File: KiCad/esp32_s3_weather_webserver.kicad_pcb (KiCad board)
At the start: 4 copper layers, 85 x 75 mm, 129 parts, among them IC301 CP2102N-A02-GQFN28R, IC401 ESP32-S3-WROOM-1-N16R8, IC501 VEML7700-TT, IC502 DS3231MZ+TRL, J201 Barrel_Jack_Switch_Pin3Ring, J301 USB_C_Receptacle_USB2.0, J302 USB_C_Receptacle_USB2.0, J401 Conn_01x04_Pin, J402 Conn_01x04_Pin, J403 Conn_01x04_Pin, J404 TF-01A, J405 Conn_01x06_Pin, Q401 SS8050, Q402 SS8050, U201 AMS1117-3.3, U202 TLV62569DBV, U301 USBLC6-2SC6, U302 USBLC6-2SC6, U502 DS18B20, U503 LM35-LP, U504 DHT11

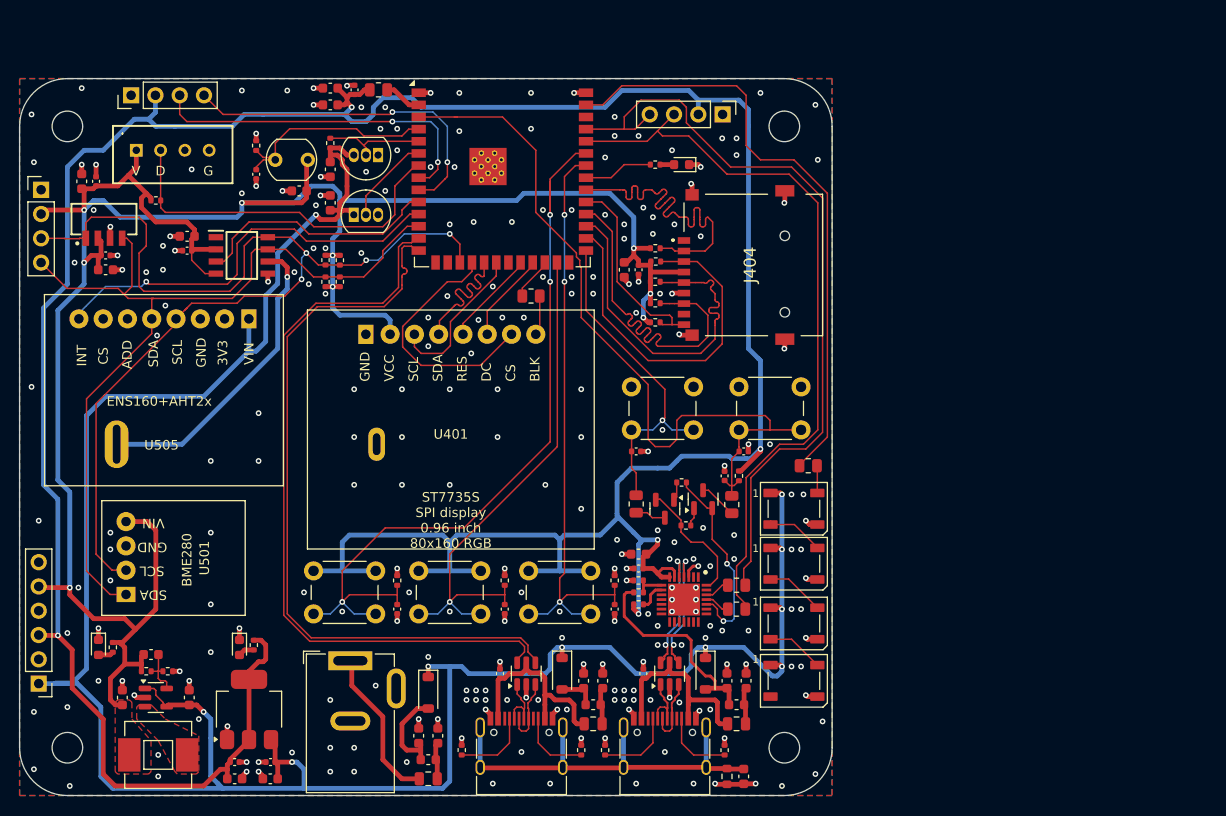
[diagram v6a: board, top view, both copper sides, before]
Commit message: Temperature sensor placement update
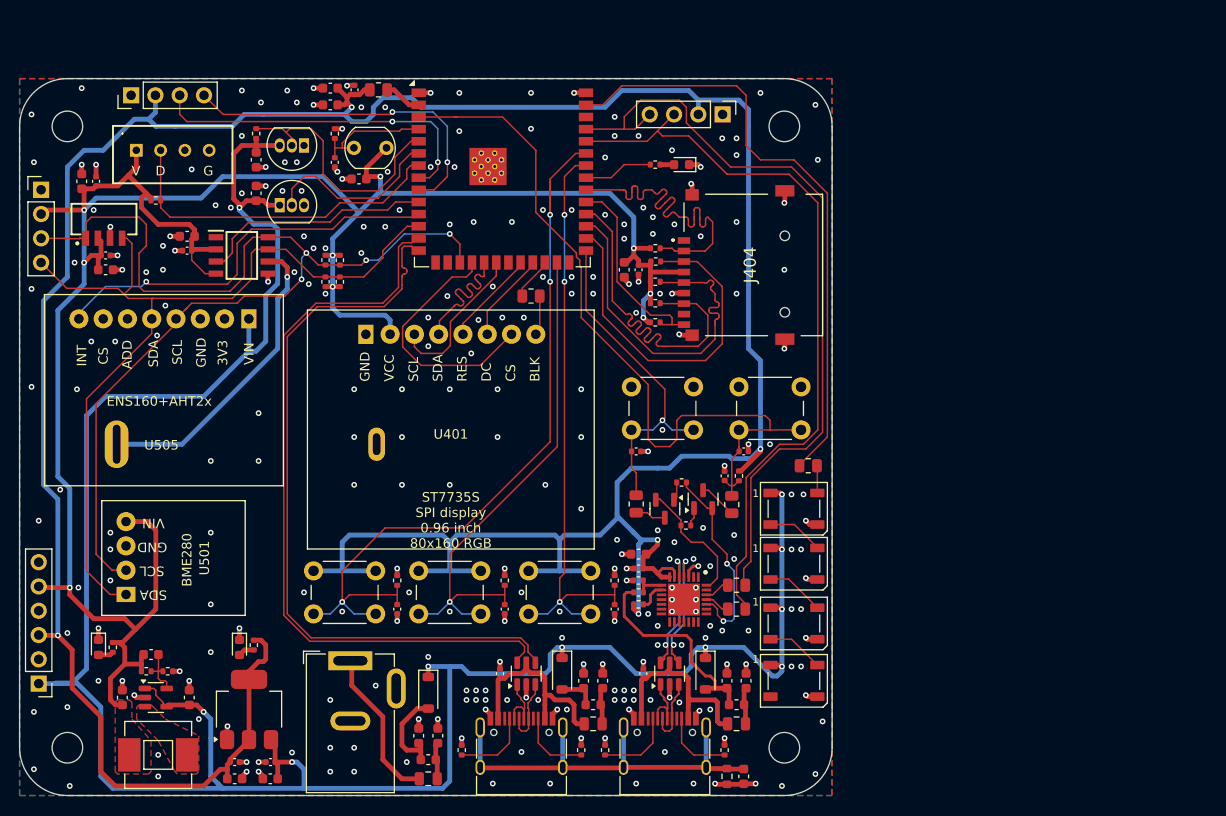
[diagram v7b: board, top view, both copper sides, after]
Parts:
- moved C502 8.32 mm to (58.0, 33.8)
- moved R501 8.32 mm to (58.0, 30.8)
- moved RLO501 8.32 mm to (60.0, 32.2)
- moved C505 7.81 mm to (49.8, 33.5)
- moved C506 7.81 mm to (49.8, 37.0)
- moved R504 7.81 mm to (49.8, 30.8)
- moved U502 7.81 mm to (54.8, 32.0)
- moved U503 7.81 mm to (52.2, 38.2)
- moved C501 6.37 mm to (60.5, 35.5)
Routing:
- net DS18B20: track 11.3 -> 26.9 mm
- net LM35: track 9.34 -> 19.1 mm
- net LDR: track 23.0 -> 13.5 mm
- net +3V3_PER: track 242.9 -> 238.3 mm
- net DHT11: track 38.2 -> 36.2 mm
- net +5V: track 249.9 -> 251.5 mm
- net DS3231_INT: track 26.0 -> 24.7 mm
- net ENS160_INT: track 43.6 -> 42.5 mm
- net GND: track 76.1 -> 76.0 mm, vias 258 -> 274

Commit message: Silk Screen updates
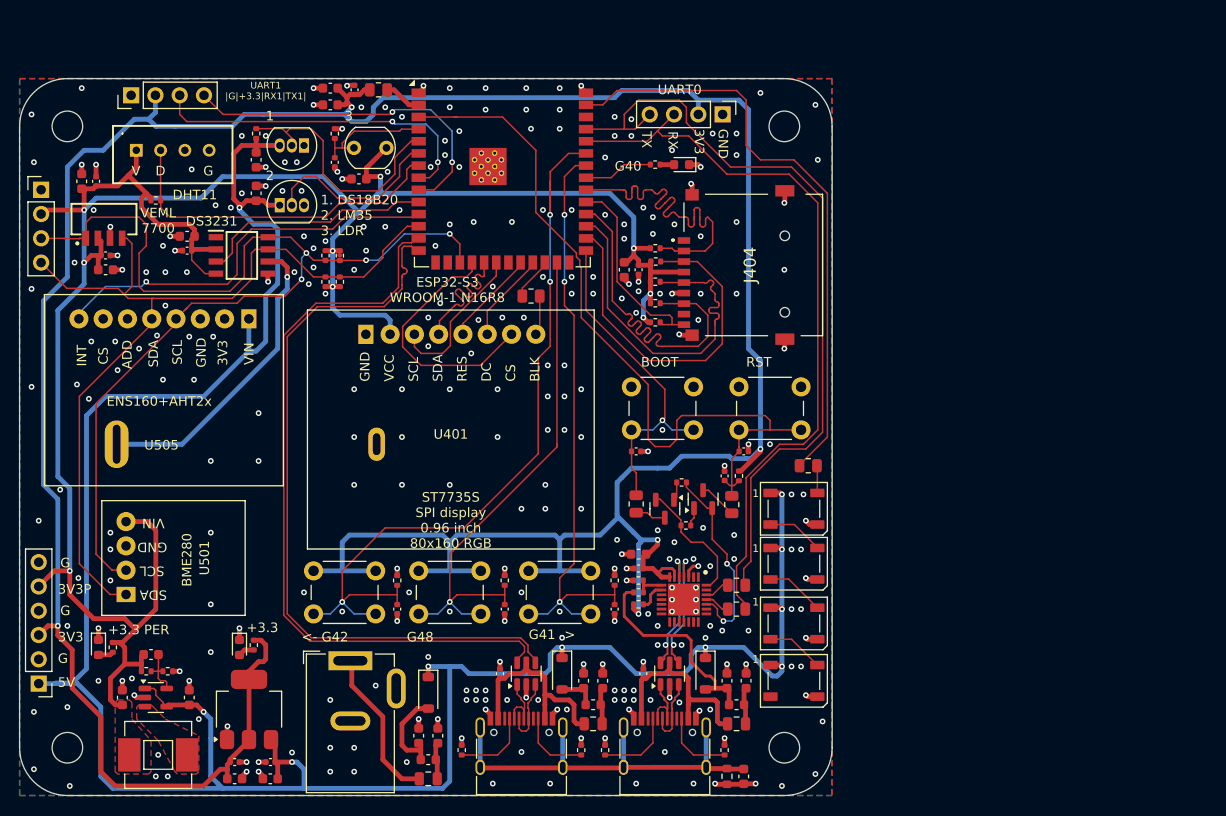
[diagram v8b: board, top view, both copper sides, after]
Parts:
- moved R502 0.48 mm to (57.0, 43.5)
- moved R507 0.48 mm to (58.5, 43.5)
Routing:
- net +3V3_PER: track 238.3 -> 239.1 mm
- net USR_BTN_RIGHT: track 63.0 -> 63.9 mm
- net WS2812_RGB_STRIP: track 63.5 -> 62.8 mm
- net GND: track 76.0 -> 75.4 mm, vias 274 -> 307
- net I2C_SDA: track 92.2 -> 92.8 mm
- net TXD1: track 35.8 -> 36.5 mm
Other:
- board text added: "+3.3"
- board text added: "+3.3 PER"
- board text added: "1"
- board text added: "1. DS18B20 2. LM35 3. LDR"
- board text added: "2"
- board text added: "3"
- board text added: "3V3"
- board text added: "3V3P"
- board text added: "5V"
- board text added: "<- G42"
- board text added: "BOOT"
- board text added: "DHT11"
- board text added: "DS3231"
- board text added: "ESP32-S3 WROOM-1 N16R8"
- board text added: "G"
- board text added: "G40"
- board text added: "G41 ->"
- board text added: "G48"
- board text added: "GND"
- board text added: "RST"
- board text added: "RX"
- board text added: "TX"
- board text added: "UART0"
- board text added: "UART1 |G|+3.3|RX1|TX1|"
- board text added: "VEML 7700"
